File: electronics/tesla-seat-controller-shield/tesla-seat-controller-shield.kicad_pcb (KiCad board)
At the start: 2 copper layers, 68.8 x 53.6 mm, 12 parts, among them J1 12V In, J2 Motor Driver, J3 Fan Upper, J4 Fan Lower, J5 Switchpack

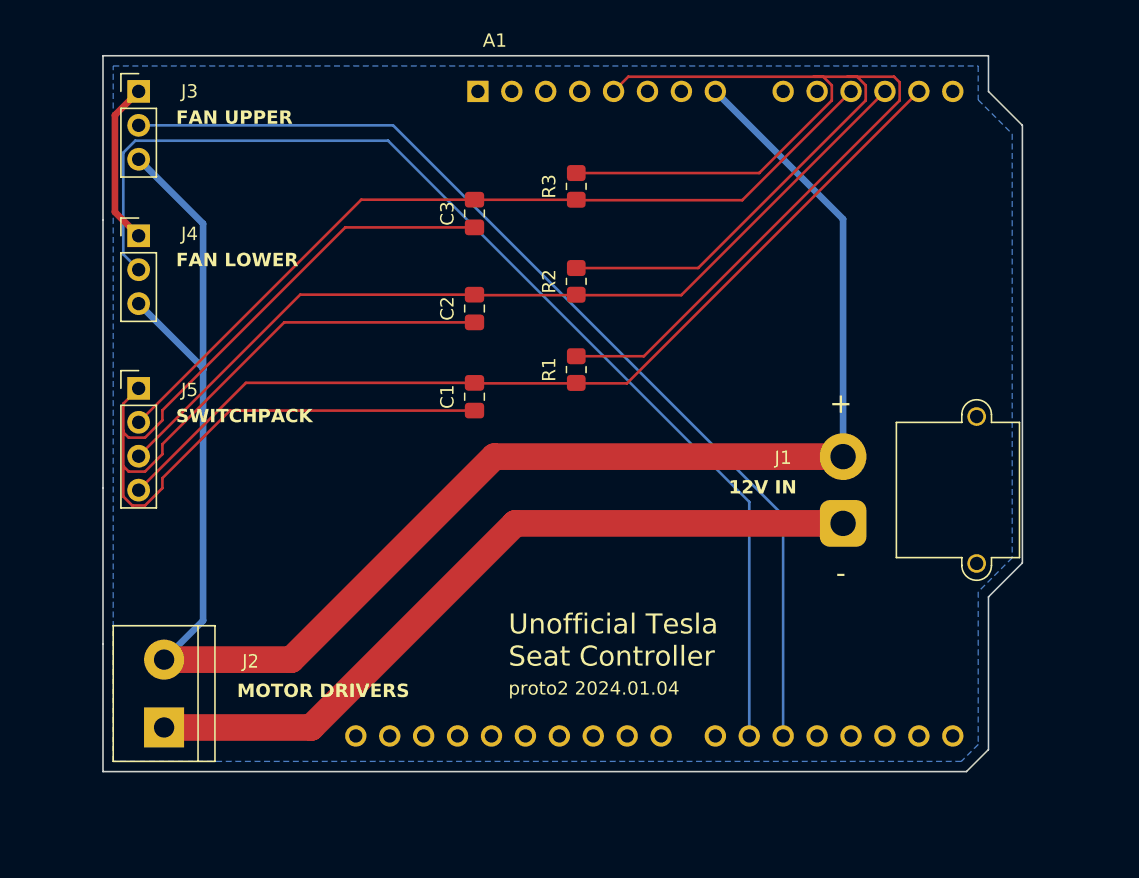
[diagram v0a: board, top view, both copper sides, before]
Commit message: Mirror Arduino shield and update some documentation paths
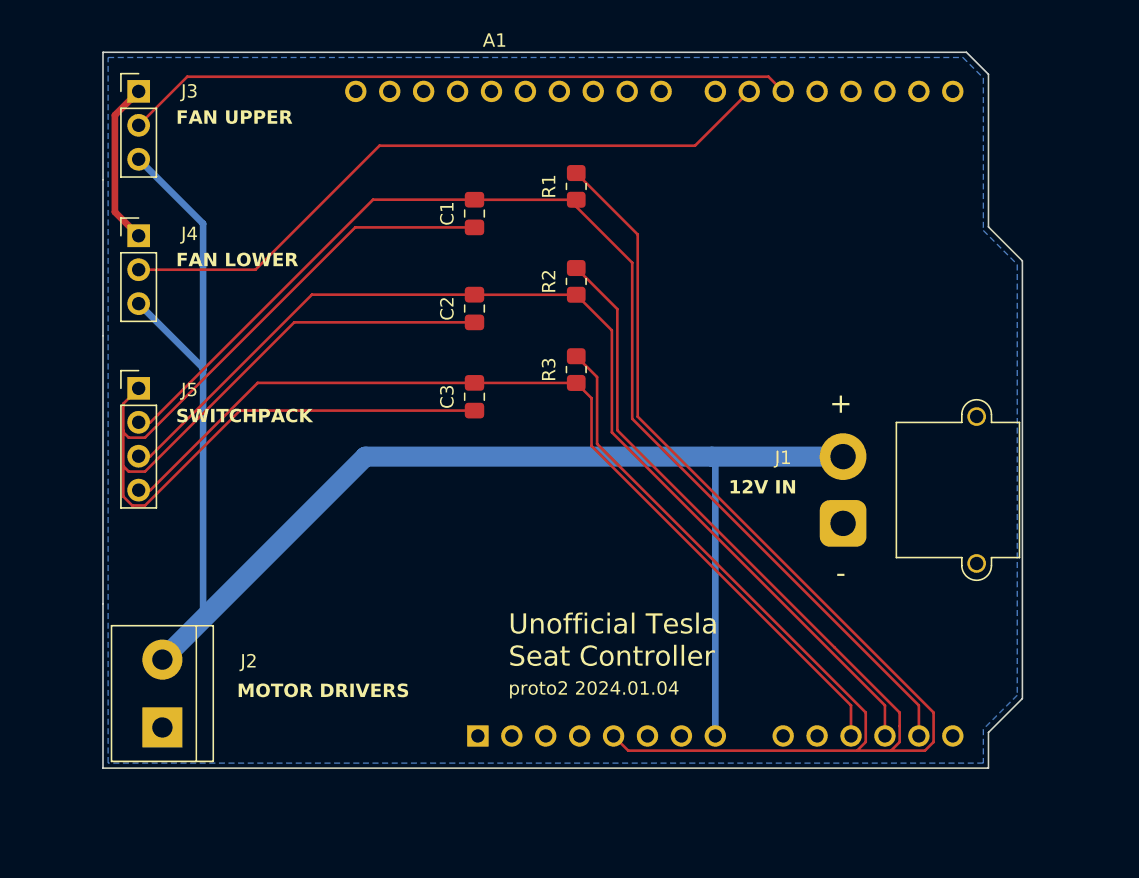
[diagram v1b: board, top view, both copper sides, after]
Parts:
- moved R1 13.7 mm to (137.7, 77.2)
- moved R3 13.7 mm to (137.7, 90.9)
- moved C1 13.7 mm to (130.0, 79.2)
- moved C3 13.7 mm to (130.0, 93.0)
- moved J2 0.13 mm to (106.7, 117.7)
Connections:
- J5 pad 2: /switch_backrest_track -> /switch_lumbar
- J5 pad 4: /switch_lumbar -> /switch_backrest_track
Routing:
- net GND: track 173.1 -> 114.6 mm
- net +5V: track 109.3 -> 163.6 mm
- net /fan_lower_pwm: track 85.2 -> 51.2 mm
- net /fan_upper_pwm: track 76.9 -> 50.2 mm
- net /switch_lumbar: track 70.8 -> 90.7 mm
- net /switch_tilt_lift: track 67.2 -> 80.4 mm
- net +12V: track 136.1 -> 126.1 mm
- net /switch_backrest_track: track 63.6 -> 71.0 mm
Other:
- outline, holes or cut-outs redrawn

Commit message: Replace silly vertical mirror with flip + 180
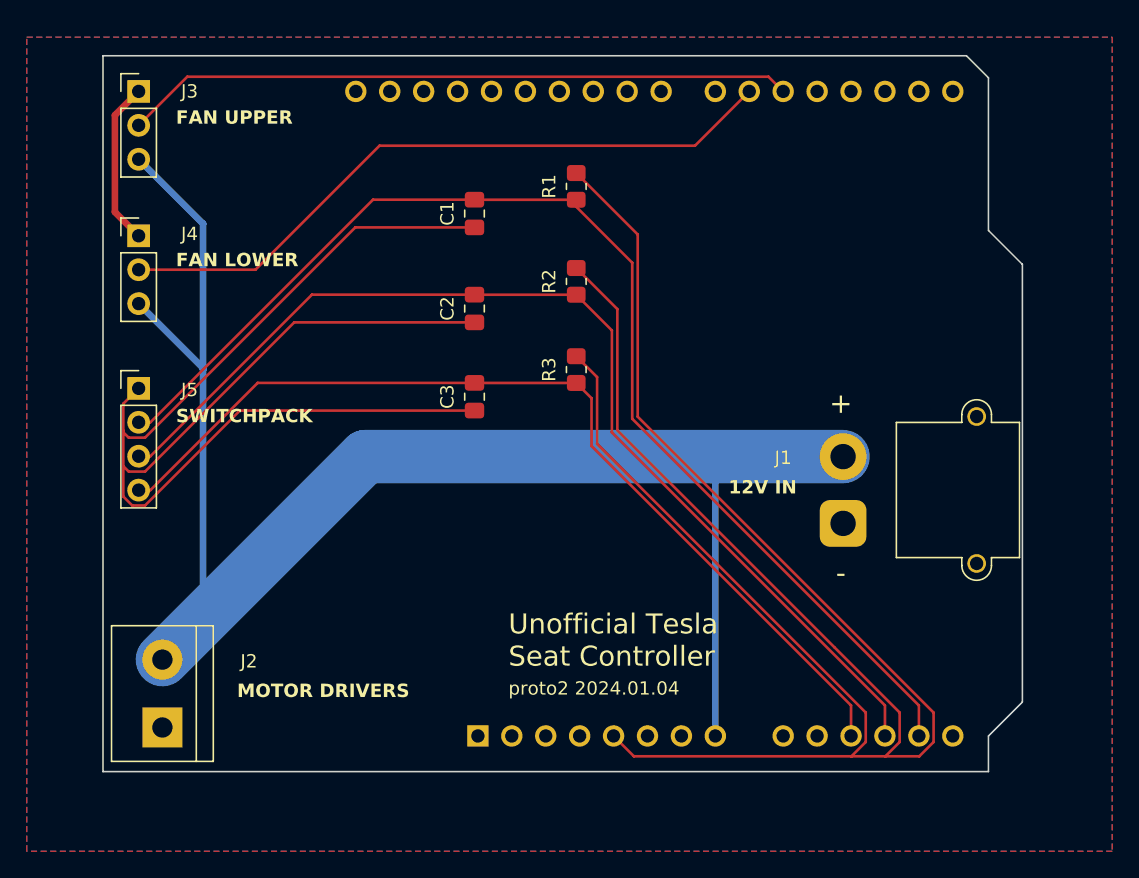
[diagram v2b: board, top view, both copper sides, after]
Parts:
- A1: moved to B.Cu
- moved A1 48.3 mm to (130.3, 118.4)
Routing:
- net +5V: track 163.6 -> 165.1 mm
- added copper zone on F.Cu, net GND
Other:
- outline, holes or cut-outs redrawn

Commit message: Add teardrops
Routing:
- net GND: track 114.6 -> 0.00 mm, vias 0 -> 2
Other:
- board text added: "proto2 2024.01.06"
- board text removed: "proto2 2024.01.04"

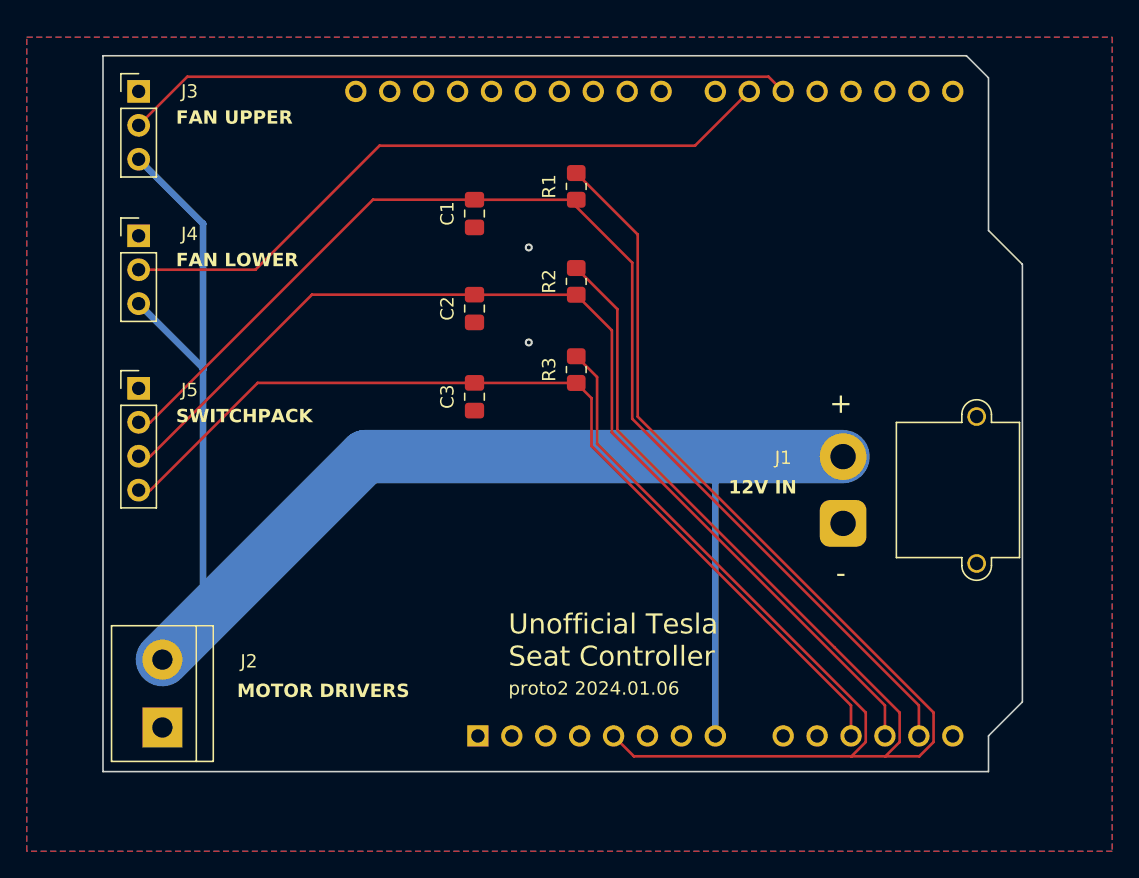
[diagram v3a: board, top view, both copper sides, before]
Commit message: Add 3D models and make board updates to match shield layout
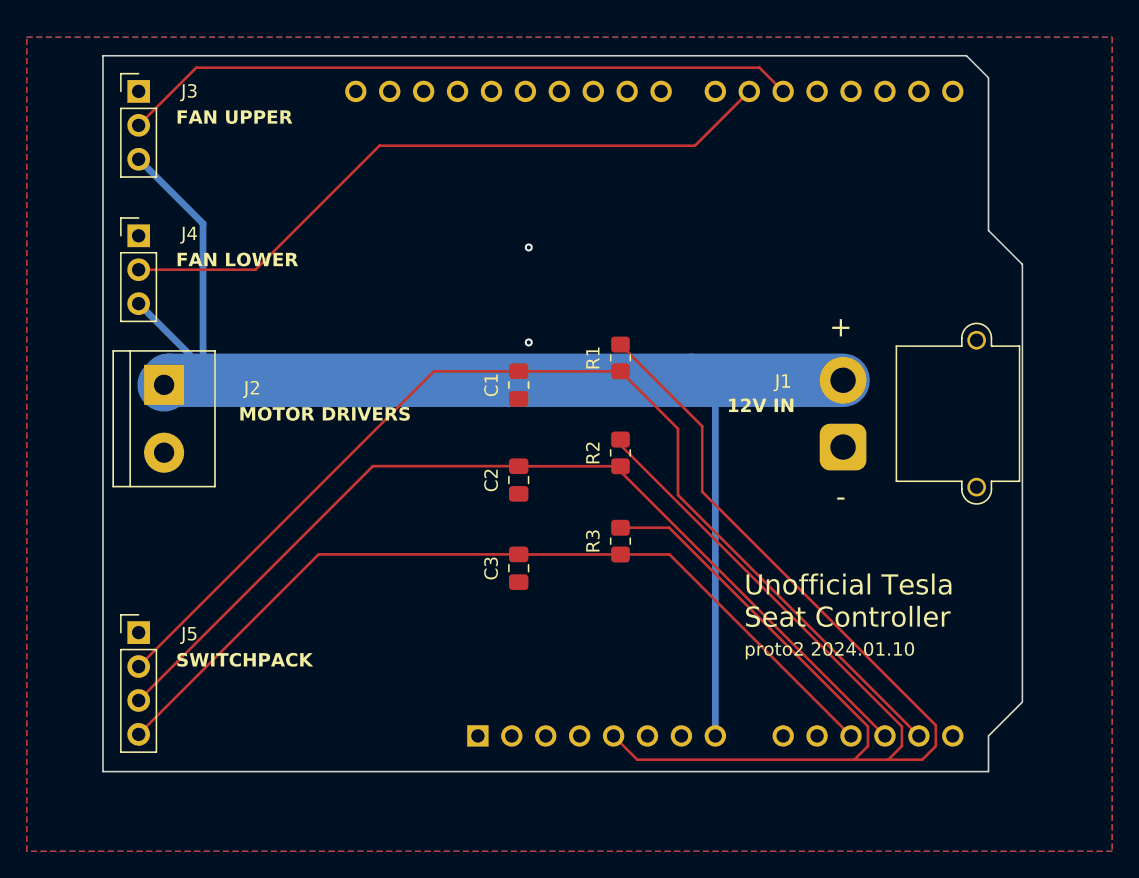
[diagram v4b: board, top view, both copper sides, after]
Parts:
- moved J2 25.7 mm to (106.8, 92.1), turned to -90 degrees
- moved J5 18.3 mm to (104.9, 110.6)
- moved C2 13.3 mm to (133.4, 99.2)
- moved C3 13.3 mm to (133.4, 105.8)
- moved R1 13.3 mm to (141.0, 90.1)
- moved R2 13.3 mm to (141.0, 97.2)
- moved R3 13.3 mm to (141.0, 103.8)
- moved C1 13.3 mm to (133.4, 92.1)
- moved J1 5.72 mm to (157.6, 96.7)
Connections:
- J2 pad 1: GND -> +12V
- J2 pad 2: +12V -> GND
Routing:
- net +5V: track 165.1 -> 125.9 mm
- net +12V: track 126.1 -> 103.0 mm
- net /switch_tilt_lift: track 80.4 -> 71.7 mm
- net /switch_lumbar: track 90.7 -> 82.1 mm
- net /switch_backrest_track: track 71.0 -> 64.6 mm
- net /fan_upper_pwm: track 50.2 -> 50.8 mm
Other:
- board text added: "proto2 2024.01.10"
- board text removed: "proto2 2024.01.06"

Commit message: Update part positions and remove 12v Vin
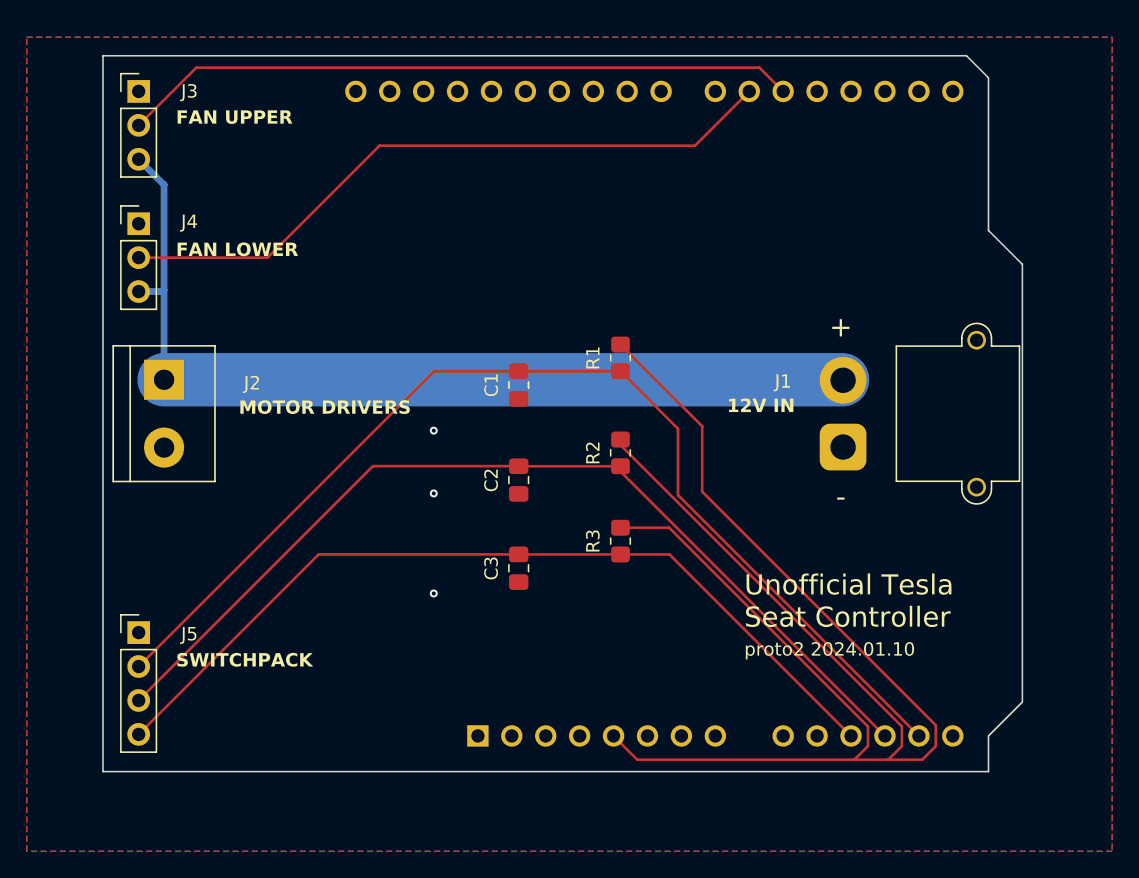
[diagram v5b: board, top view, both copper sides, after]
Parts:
- moved J4 0.90 mm to (104.9, 80.0)
- moved J2 0.38 mm to (106.8, 91.7)
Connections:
- A1 pad 8: +12V -> unconnected-(A1-VIN-Pad8)
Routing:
- net +12V: track 103.0 -> 70.1 mm
- net GND: vias 2 -> 3
